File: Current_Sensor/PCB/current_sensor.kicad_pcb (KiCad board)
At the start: 2 copper layers, 39 x 25 mm, 25 parts, among them J4 DS conn, T2 TRANS-2CT, U1 Buffer, U3 AMC1303, U5 SN6501DBV, U7 TPS76350

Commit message: files reordering
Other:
- board size 39 x 25 mm -> 40 x 25 mm
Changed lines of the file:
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@@
   )
   (setup
-    (last_trace_width 1)
+    (last_trace_width 0.25)
     (user_trace_width 0.5)
     (user_trace_width 1)
@@
   )
   (gr_line (start 133 97) (end 133 72) (layer Edge.Cuts) (width 0.2))
-  (gr_line (start 172 97) (end 133 97) (layer Edge.Cuts) (width 0.2))
-  (gr_line (start 172 72) (end 172 97) (layer Edge.Cuts) (width 0.2))
-  (gr_line (start 133 72) (end 172 72) (layer Edge.Cuts) (width 0.2))
+  (gr_line (start 173 97) (end 133 97) (layer Edge.Cuts) (width 0.2))
+  (gr_line (start 173 72) (end 173 97) (layer Edge.Cuts) (width 0.2))
+  (gr_line (start 133 72) (end 173 72) (layer Edge.Cuts) (width 0.2))
   (segment (start 163.6 75.35) (end 163.16 75.35) (width 0.5) (layer F.Cu) (net 1) (status 30))
   (segment (start 163.16 75.35) (end 161.57 73.76) (width 0.5) (layer F.Cu) (net 1) (status 30))

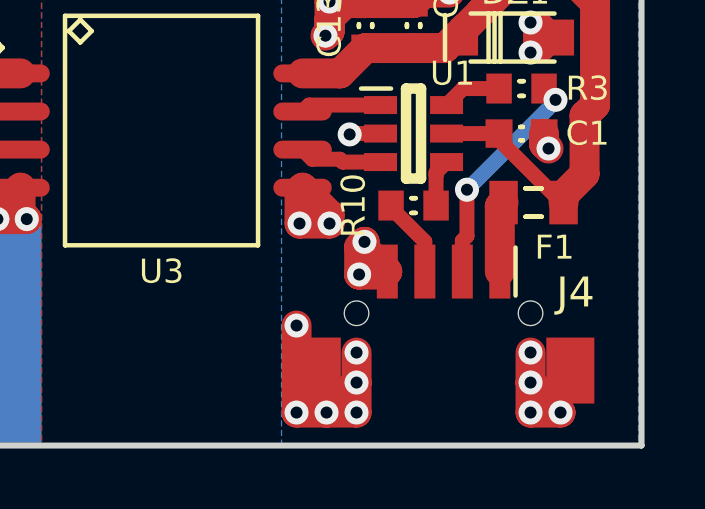
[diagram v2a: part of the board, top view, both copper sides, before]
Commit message: Update current sensor connector + LTC6811
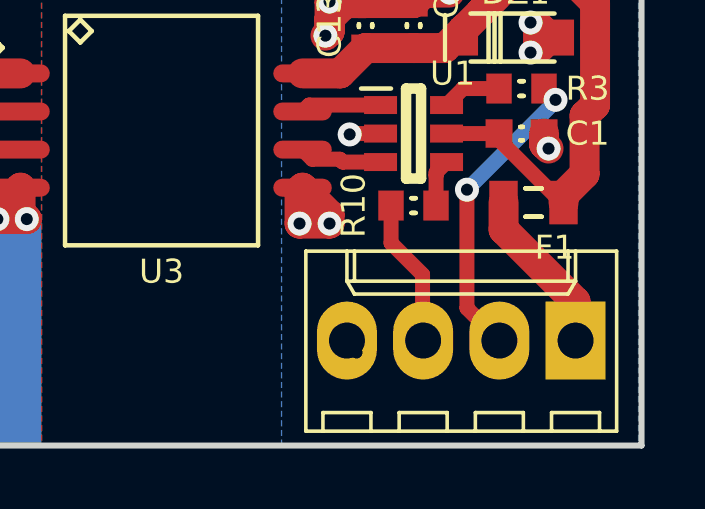
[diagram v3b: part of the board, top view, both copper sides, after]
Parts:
- J4: footprint paltatech:DF13-4P-1.25H(50) -> Connectors_Molex:Molex_KK-6410-04_04x2.54mm_Straight
- R1: value 0.035uOhm -> 0.035mOhm
- moved J4 4.51 mm to (170.8, 93.5)
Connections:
- U7 pad 4: (no net) -> Net-(U7-Pad4)
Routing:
- net GND: track 44.8 -> 28.3 mm, vias 25 -> 14
- net Net-(F1-Pad1): track 2.39 -> 5.63 mm
- net /delta_sigma: track 7.65 -> 10.3 mm
- net /clk: track 2.67 -> 4.94 mm
